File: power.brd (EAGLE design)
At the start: 90.2 x 95.9 mm, 0 parts

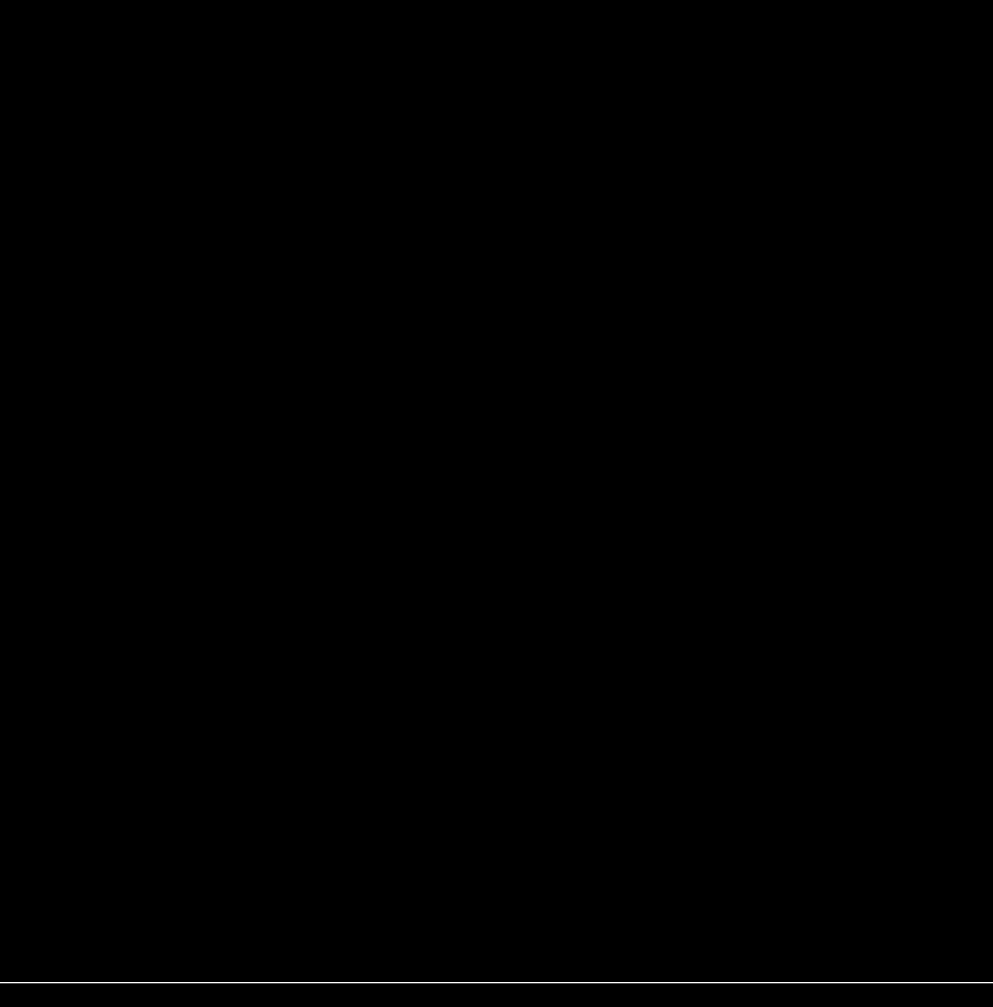
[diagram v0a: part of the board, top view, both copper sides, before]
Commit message: Added solar panel libraries
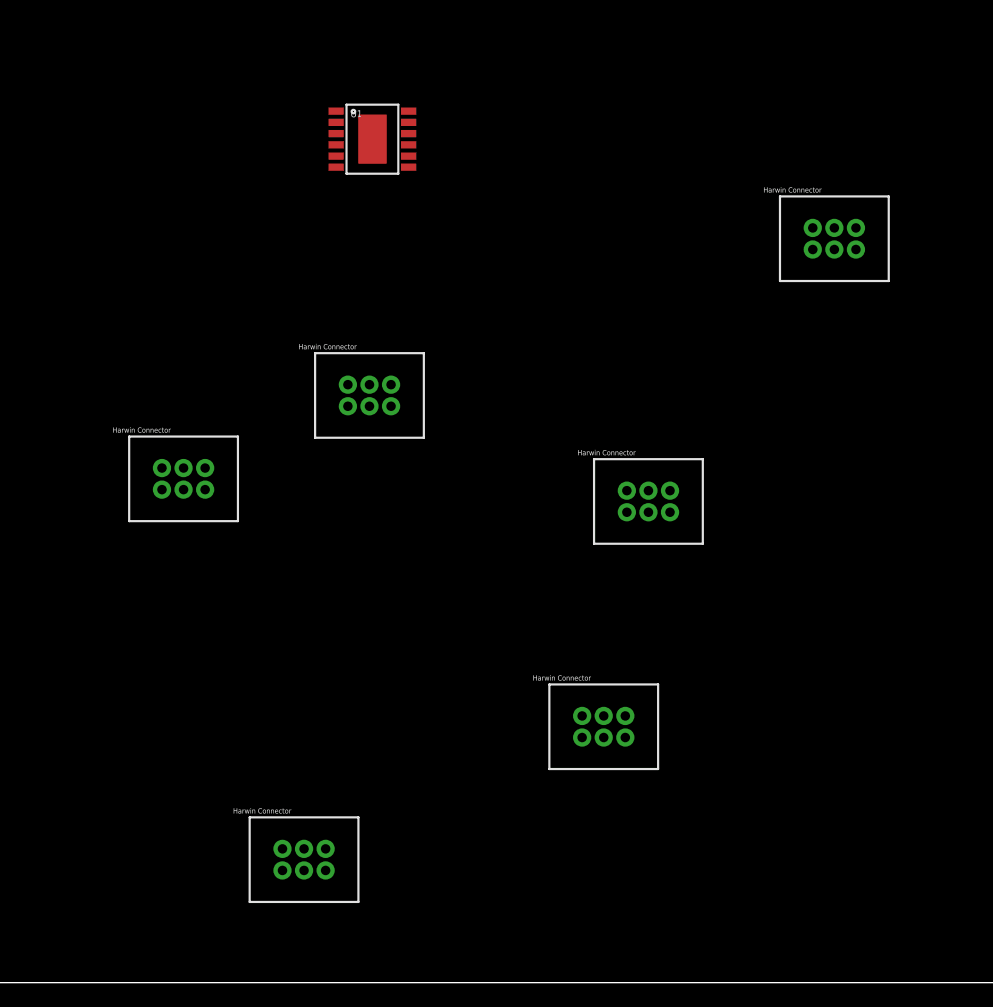
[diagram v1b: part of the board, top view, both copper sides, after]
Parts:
- added U$1, U$2, U$3, U$4, U$5, U$6: G125-FV20605L0P, G125-FV20605L0P:G125-FV20605L0P
- added U1: LT3652, SparkFun-PowerIC:MSOP-12_GND
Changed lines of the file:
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@@
 <?xml version="1.0" encoding="utf-8"?>
 <!DOCTYPE eagle SYSTEM "eagle.dtd">
-<eagle version="6.5.0">
+<eagle version="6.6.0">
 <drawing>
 <settings>
@@
 </autorouter>
 <elements>
+<element name="U1" library="SparkFun-PowerIC" package="MSOP-12_GND" value="LT3652" x="31.78" y="48.86"/>
+<element name="U$1" library="G125-FV20605L0P" package="G125-FV20605L0P" value="G125-FV20605L0P" x="44.57" y="25.35"/>
+<element name="U$2" library="G125-FV20605L0P" package="G125-FV20605L0P" value="G125-FV20605L0P" x="17.64" y="26.66"/>
+<element name="U$3" library="G125-FV20605L0P" package="G125-FV20605L0P" value="G125-FV20605L0P" x="24.62" y="4.6"/>
+<element name="U$4" library="G125-FV20605L0P" package="G125-FV20605L0P" value="G125-FV20605L0P" x="41.98" y="12.3"/>
+<element name="U$5" library="G125-FV20605L0P" package="G125-FV20605L0P" value="G125-FV20605L0P" x="55.34" y="40.57"/>
+<element name="U$6" library="G125-FV20605L0P" package="G125-FV20605L0P" value="G125-FV20605L0P" x="28.41" y="31.49"/>
 </elements>
 <signals>

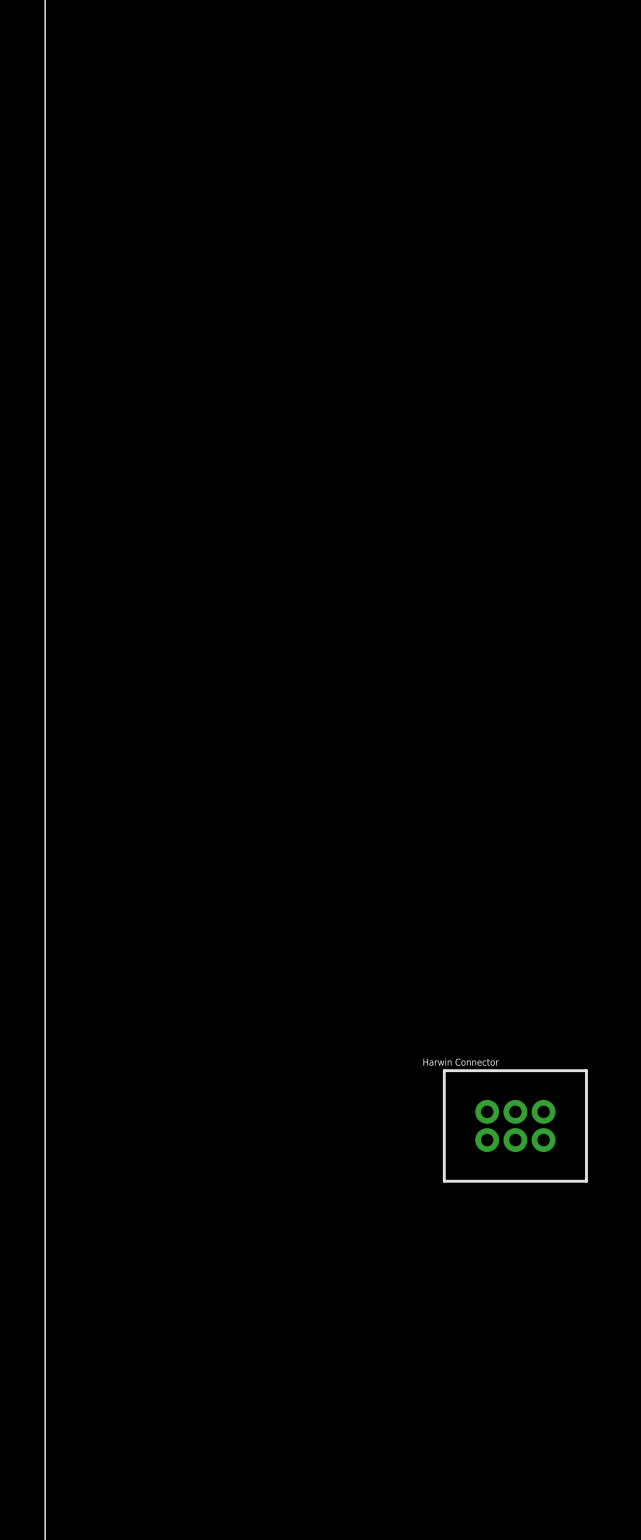
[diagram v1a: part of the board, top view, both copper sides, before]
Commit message: Added RTC backup batteries
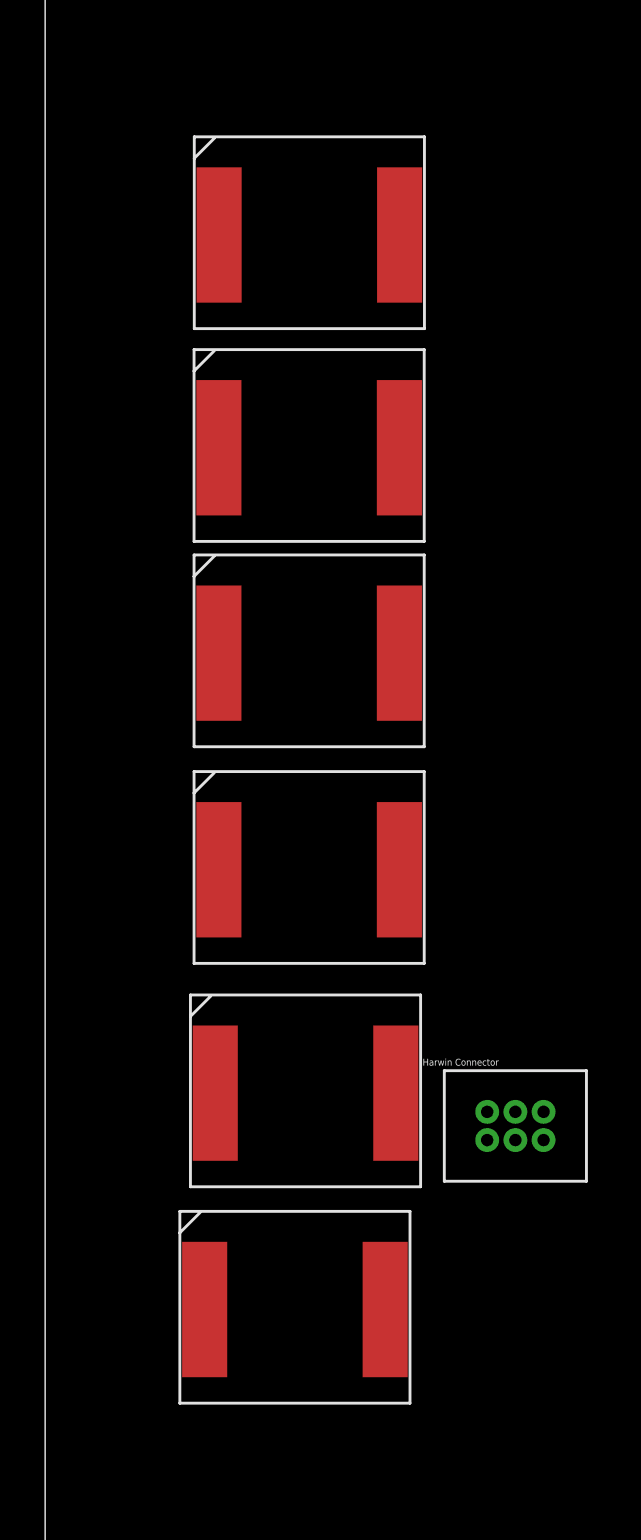
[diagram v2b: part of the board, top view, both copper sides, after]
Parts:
- added U$10, U$11, U$12, U$7, U$8, U$9: BETABATTERY, Widetronix:BETABATTERY
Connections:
- new net V+: U$10.V+, U$11.V+, U$12.V+, U$7.V+, U$8.V+, U$9.V+
- new net V-: U$10.V-, U$11.V-, U$12.V-, U$7.V-, U$8.V-, U$9.V-
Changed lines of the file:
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@@
 <element name="U$5" library="G125-FV20605L0P" package="G125-FV20605L0P" value="G125-FV20605L0P" x="55.34" y="40.57"/>
 <element name="U$6" library="G125-FV20605L0P" package="G125-FV20605L0P" value="G125-FV20605L0P" x="28.41" y="31.49"/>
+<element name="U$7" library="Widetronix" package="BETABATTERY" value="BETABATTERY" x="11.71" y="68.77"/>
+<element name="U$8" library="Widetronix" package="BETABATTERY" value="BETABATTERY" x="11.7" y="59.34"/>
+<element name="U$9" library="Widetronix" package="BETABATTERY" value="BETABATTERY" x="11.7" y="50.24"/>
+<element name="U$10" library="Widetronix" package="BETABATTERY" value="BETABATTERY" x="11.7" y="40.64"/>
+<element name="U$11" library="Widetronix" package="BETABATTERY" value="BETABATTERY" x="11.54" y="30.74"/>
+<element name="U$12" library="Widetronix" package="BETABATTERY" value="BETABATTERY" x="11.07" y="21.15"/>
 </elements>
 <signals>
@@
 <via x="5.09" y="5.08" extent="1-16" drill="3.175" diameter="5"/>
 </signal>
+<signal name="V+">
+<contactref element="U$7" pad="V+"/>
+<contactref element="U$8" pad="V+"/>
+<contactref element="U$9" pad="V+"/>
+<contactref element="U$10" pad="V+"/>
+<contactref element="U$11" pad="V+"/>
+<contactref element="U$12" pad="V+"/>
+<wire x1="7.54" y1="30.64" x2="7.07" y2="21.05" width="0" layer="19" extent="1-1"/>
+<wire x1="7.7" y1="40.54" x2="7.54" y2="30.64" width="0" layer="19" extent="1-1"/>
+<wire x1="7.7" y1="50.14" x2="7.7" y2="40.54" width="0" layer="19" extent="1-1"/>
+<wire x1="7.7" y1="59.24" x2="7.7" y2="50.14" width="0" layer="19" extent="1-1"/>
+<wire x1="7.71" y1="68.67" x2="7.7" y2="59.24" width="0" layer="19" extent="1-1"/>
+</signal>
+<signal name="V-">
+<contactref element="U$7" pad="V-"/>
+<contactref element="U$8" pad="V-"/>
+<contactref element="U$9" pad="V-"/>
+<contactref element="U$10" pad="V-"/>
+<contactref element="U$11" pad="V-"/>
+<contactref element="U$12" pad="V-"/>
+<wire x1="15.54" y1="30.64" x2="15.07" y2="21.05" width="0" layer="19" extent="1-1"/>
+<wire x1="15.7" y1="40.54" x2="15.54" y2="30.64" width="0" layer="19" extent="1-1"/>
+<wire x1="15.7" y1="50.14" x2="15.7" y2="40.54" width="0" layer="19" extent="1-1"/>
+<wire x1="15.7" y1="59.24" x2="15.7" y2="50.14" width="0" layer="19" extent="1-1"/>
+<wire x1="15.71" y1="68.67" x2="15.7" y2="59.24" width="0" layer="19" extent="1-1"/>
+</signal>
 </signals>

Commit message: Power board work
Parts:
- added H1, H2: PINHD-2X26, SparkFun-Connectors:2X26
- added J1: POWER_JACKPTH_BREAD, SparkFun-Connectors:POWER_JACK_PTH_BREAD
- added JP1, JP2, JP3: M025MM, SparkFun-Connectors:SCREWTERMINAL-5MM-2
- moved U$2 55.4 mm to (70.1, 44.3)
- moved U$4 21.2 mm to (41.7, 33.5)
- moved U1 19.7 mm to (48.3, 59.7)
- moved U$3 14.5 mm to (29.9, 18.1)
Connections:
- removed net V+: U$10.V+, U$11.V+, U$12.V+, U$7.V+, U$8.V+, U$9.V+
- removed net V-: U$10.V-, U$11.V-, U$12.V-, U$7.V-, U$8.V-, U$9.V-
- new net 3.3V: H2.27, H2.28
- new net 5V: H2.25, H2.26
- new net GND: H2.29, H2.30, H2.31, H2.32, J1.GND, J1.GNDBREAK, JP1.1, JP2.1, JP3.1, U$10.V-, U$11.V-, U$12.V-, U$7.V-, U$8.V-, U$9.V-, U1.13
- new net SCL: H1.43
- new net SDA: H1.41
- new net VBACKUP: H1.42, U$10.V+, U$11.V+, U$12.V+, U$7.V+, U$8.V+, U$9.V+
- new net VBATT: H2.45, H2.46, J1.PWR, JP1.2, JP2.2
- new net VBURN3: JP3.2
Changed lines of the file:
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@@
 </autorouter>
 <elements>
-<element name="U1" library="SparkFun-PowerIC" package="MSOP-12_GND" value="LT3652" x="31.78" y="48.86"/>
+<element name="U1" library="SparkFun-PowerIC" package="MSOP-12_GND" value="LT3652" x="48.27" y="59.69"/>
 <element name="U$1" library="G125-FV20605L0P" package="G125-FV20605L0P" value="G125-FV20605L0P" x="44.57" y="25.35"/>
-<element name="U$2" library="G125-FV20605L0P" package="G125-FV20605L0P" value="G125-FV20605L0P" x="17.64" y="26.66"/>
-<element name="U$3" library="G125-FV20605L0P" package="G125-FV20605L0P" value="G125-FV20605L0P" x="24.62" y="4.6"/>
-<element name="U$4" library="G125-FV20605L0P" package="G125-FV20605L0P" value="G125-FV20605L0P" x="41.98" y="12.3"/>
+<element name="U$2" library="G125-FV20605L0P" package="G125-FV20605L0P" value="G125-FV20605L0P" x="70.14" y="44.32"/>
+<element name="U$3" library="G125-FV20605L0P" package="G125-FV20605L0P" value="G125-FV20605L0P" x="29.92" y="18.08"/>
+<element name="U$4" library="G125-FV20605L0P" package="G125-FV20605L0P" value="G125-FV20605L0P" x="41.68" y="33.49"/>
 <element name="U$5" library="G125-FV20605L0P" package="G125-FV20605L0P" value="G125-FV20605L0P" x="55.34" y="40.57"/>
 <element name="U$6" library="G125-FV20605L0P" package="G125-FV20605L0P" value="G125-FV20605L0P" x="28.41" y="31.49"/>
@@
 <element name="U$11" library="Widetronix" package="BETABATTERY" value="BETABATTERY" x="11.54" y="30.74"/>
 <element name="U$12" library="Widetronix" package="BETABATTERY" value="BETABATTERY" x="11.07" y="21.15"/>
+<element name="J1" library="SparkFun-Connectors" package="POWER_JACK_PTH_BREAD" value="POWER_JACKPTH_BREAD" x="45.085" y="-3">
+<attribute name="PROD_ID" value="PRT-10811" x="45.085" y="-3" size="1.778" layer="27" display="off"/>
+</element>
+<element name="JP1" library="SparkFun-Connectors" package="SCREWTERMINAL-5MM-2" value="M025MM" x="75.98" y="29.87"/>
+<element name="JP2" library="SparkFun-Connectors" package="SCREWTERMINAL-5MM-2" value="M025MM" x="25.26" y="72.44"/>
+<element name="JP3" library="SparkFun-Connectors" package="SCREWTERMINAL-5MM-2" value="M025MM" x="64.43" y="65.94"/>
+<element name="H1" library="SparkFun-Connectors" package="2X26" value="PINHD-2X26" x="25.4" y="84.46"/>
+<element name="H2" library="SparkFun-Connectors" package="2X26" value="PINHD-2X26" x="25.4" y="89.54"/>
 </elements>
 <signals>
@@
 <via x="85.09" y="5.08" extent="1-16" drill="3.175" diameter="5"/>
 <via x="5.09" y="5.08" extent="1-16" drill="3.175" diameter="5"/>
+<contactref element="U1" pad="13"/>
+<contactref element="U$7" pad="V-"/>
+<contactref element="U$8" pad="V-"/>
+<contactref element="U$9" pad="V-"/>
+<contactref element="U$10" pad="V-"/>
+<contactref element="U$11" pad="V-"/>
+<contactref element="U$12" pad="V-"/>
+<contactref element="J1" pad="GND"/>
+<contactref element="J1" pad="GNDBREAK"/>
+<contactref element="JP1" pad="1"/>
+<contactref element="JP2" pad="1"/>
+<contactref element="JP3" pad="1"/>
+<contactref element="H2" pad="29"/>
+<contactref element="H2" pad="31"/>
+<contactref element="H2" pad="30"/>
+<contactref element="H2" pad="32"/>
+<wire x1="49.885" y1="7.7" x2="82.55" y2="90.805" width="0" layer="19" extent="1-1"/>
+<wire x1="45.085" y1="4.9" x2="49.885" y2="7.7" width="0" layer="19" extent="1-1"/>
+<wire x1="25.26" y1="72.44" x2="45.085" y2="4.9" width="0" layer="19" extent="1-1"/>
+<wire x1="48.27" y1="59.69" x2="25.26" y2="72.44" width="0" layer="19" extent="1-1"/>
+<wire x1="15.7" y1="50.14" x2="48.27" y2="59.69" width="0" layer="19" extent="1-1"/>
+<wire x1="15.7" y1="59.24" x2="15.7" y2="50.14" width="0" layer="19" extent="1-1"/>
+<wire x1="15.71" y1="68.67" x2="15.7" y2="59.24" width="0" layer="19" extent="1-1"/>
+<wire x1="15.7" y1="40.54" x2="15.7" y2="50.14" width="0" layer="19" extent="1-1"/>
+<wire x1="15.54" y1="30.64" x2="15.7" y2="40.54" width="0" layer="19" extent="1-1"/>
+<wire x1="15.07" y1="21.05" x2="15.54" y2="30.64" width="0" layer="19" extent="1-1"/>
+<wire x1="5.09" y1="5.08" x2="15.07" y2="21.05" width="0" layer="19" extent="1-1"/>
+<wire x1="64.43" y1="65.94" x2="5.09" y2="5.08" width="0" layer="19" extent="1-1"/>
+<wire x1="8.89" y1="90.805" x2="15.71" y2="68.67" width="0" layer="19" extent="1-1"/>
+<wire x1="75.98" y1="29.87" x2="45.085" y2="4.9" width="0" layer="19" extent="1-1"/>
+<wire x1="85.09" y1="5.08" x2="75.98" y2="29.87" width="0" layer="19" extent="1-1"/>
+<wire x1="49.53" y1="90.81" x2="64.43" y2="65.94" width="0" layer="19" extent="1-1"/>
+<wire x1="52.07" y1="90.81" x2="49.53" y2="90.81" width="0" layer="19" extent="1-1"/>
+<wire x1="52.07" y1="88.27" x2="52.07" y2="90.81" width="0" layer="19" extent="1-1"/>
+<wire x1="49.53" y1="88.27" x2="49.53" y2="90.81" width="0" layer="19" extent="1-1"/>
 </signal>
-<signal name="V+">
+<signal name="VBACKUP">
 <contactref element="U$7" pad="V+"/>
 <contactref element="U$8" pad="V+"/>
@@
 <contactref element="U$11" pad="V+"/>
 <contactref element="U$12" pad="V+"/>
-<wire x1="7.54" y1="30.64" x2="7.07" y2="21.05" width="0" layer="19" extent="1-1"/>
-<wire x1="7.7" y1="40.54" x2="7.54" y2="30.64" width="0" layer="19" extent="1-1"/>
-<wire x1="7.7" y1="50.14" x2="7.7" y2="40.54" width="0" layer="19" extent="1-1"/>
-<wire x1="7.7" y1="59.24" x2="7.7" y2="50.14" width="0" layer="19" extent="1-1"/>
-<wire x1="7.71" y1="68.67" x2="7.7" y2="59.24" width="0" layer="19" extent="1-1"/>
+<contactref element="H1" pad="42"/>
+<wire x1="7.7" y1="59.24" x2="7.71" y2="68.67" width="0" layer="19" extent="1-1"/>
+<wire x1="7.7" y1="50.14" x2="7.7" y2="59.24" width="0" layer="19" extent="1-1"/>
+<wire x1="7.7" y1="40.54" x2="7.7" y2="50.14" width="0" layer="19" extent="1-1"/>
+<wire x1="7.54" y1="30.64" x2="7.7" y2="40.54" width="0" layer="19" extent="1-1"/>
+<wire x1="7.07" y1="21.05" x2="7.54" y2="30.64" width="0" layer="19" extent="1-1"/>
+<wire x1="64.77" y1="85.73" x2="7.07" y2="21.05" width="0" layer="19" extent="1-1"/>
 </signal>
-<signal name="V-">
-<contactref element="U$7" pad="V-"/>
-<contactref element="U$8" pad="V-"/>
-<contactref element="U$9" pad="V-"/>
-<contactref element="U$10" pad="V-"/>
-<contactref element="U$11" pad="V-"/>
-<contactref element="U$12" pad="V-"/>
-<wire x1="15.54" y1="30.64" x2="15.07" y2="21.05" width="0" layer="19" extent="1-1"/>
-<wire x1="15.7" y1="40.54" x2="15.54" y2="30.64" width="0" layer="19" extent="1-1"/>
-<wire x1="15.7" y1="50.14" x2="15.7" y2="40.54" width="0" layer="19" extent="1-1"/>
-<wire x1="15.7" y1="59.24" x2="15.7" y2="50.14" width="0" layer="19" extent="1-1"/>
-<wire x1="15.71" y1="68.67" x2="15.7" y2="59.24" width="0" layer="19" extent="1-1"/>
+<signal name="VBATT">
+<contactref element="J1" pad="PWR"/>
+<contactref element="JP1" pad="2"/>
+<contactref element="JP2" pad="2"/>
+<contactref element="H2" pad="45"/>
+<contactref element="H2" pad="46"/>
+<wire x1="30.26" y1="72.44" x2="45.085" y2="10.7" width="0" layer="19" extent="1-1"/>
+<wire x1="80.98" y1="29.87" x2="45.085" y2="10.7" width="0" layer="19" extent="1-1"/>
+<wire x1="69.85" y1="90.81" x2="80.98" y2="29.87" width="0" layer="19" extent="1-1"/>
+<wire x1="69.85" y1="88.27" x2="69.85" y2="90.81" width="0" layer="19" extent="1-1"/>
+</signal>
+<signal name="VBURN3">
+<contactref element="JP3" pad="2"/>
+</signal>
+<signal name="SCL">
+<contactref element="H1" pad="43"/>
+</signal>
+<signal name="SDA">
+<contactref element="H1" pad="41"/>
+</signal>
+<signal name="3.3V">
+<contactref element="H2" pad="27"/>
+<contactref element="H2" pad="28"/>
+<wire x1="46.99" y1="88.27" x2="46.99" y2="90.81" width="0" layer="19" extent="1-1"/>
+</signal>
+<signal name="5V">
+<contactref element="H2" pad="25"/>
+<contactref element="H2" pad="26"/>
+<wire x1="44.45" y1="88.27" x2="44.45" y2="90.81" width="0" layer="19" extent="1-1"/>
 </signal>
 </signals>
